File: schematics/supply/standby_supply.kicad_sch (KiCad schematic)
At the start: 38 parts, among them Q10 IRLML5203, U3 R7731, U4 EL817, U5 TL431DBV

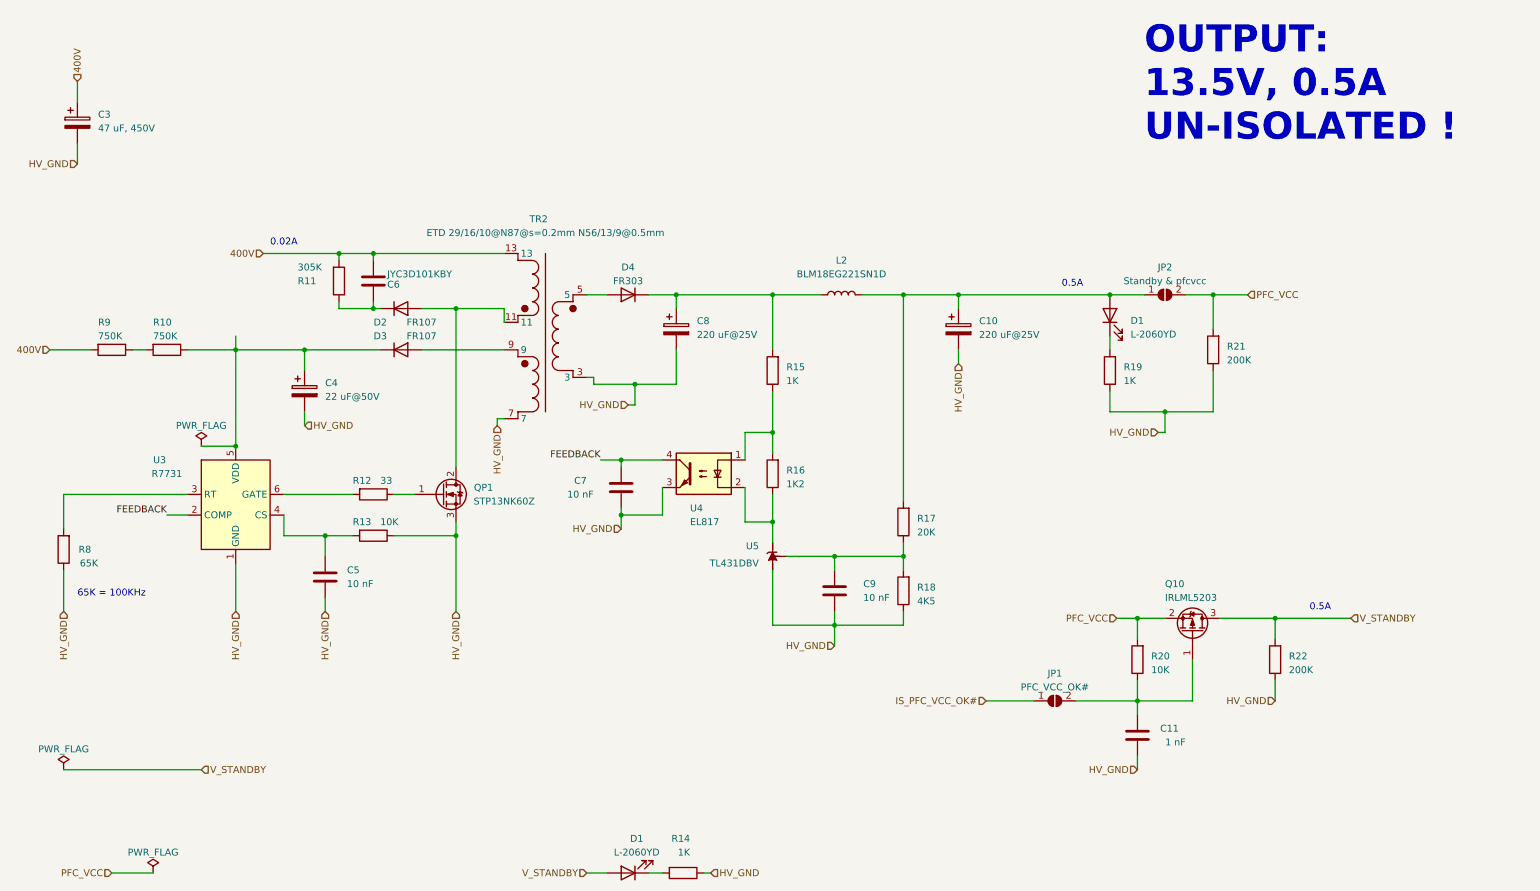
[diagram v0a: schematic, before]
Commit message: prepare to replace ina228 to attiny16+ina169(?). ina228 is an intresting chip, but its too expensive and Im not sure I can buy it on ali
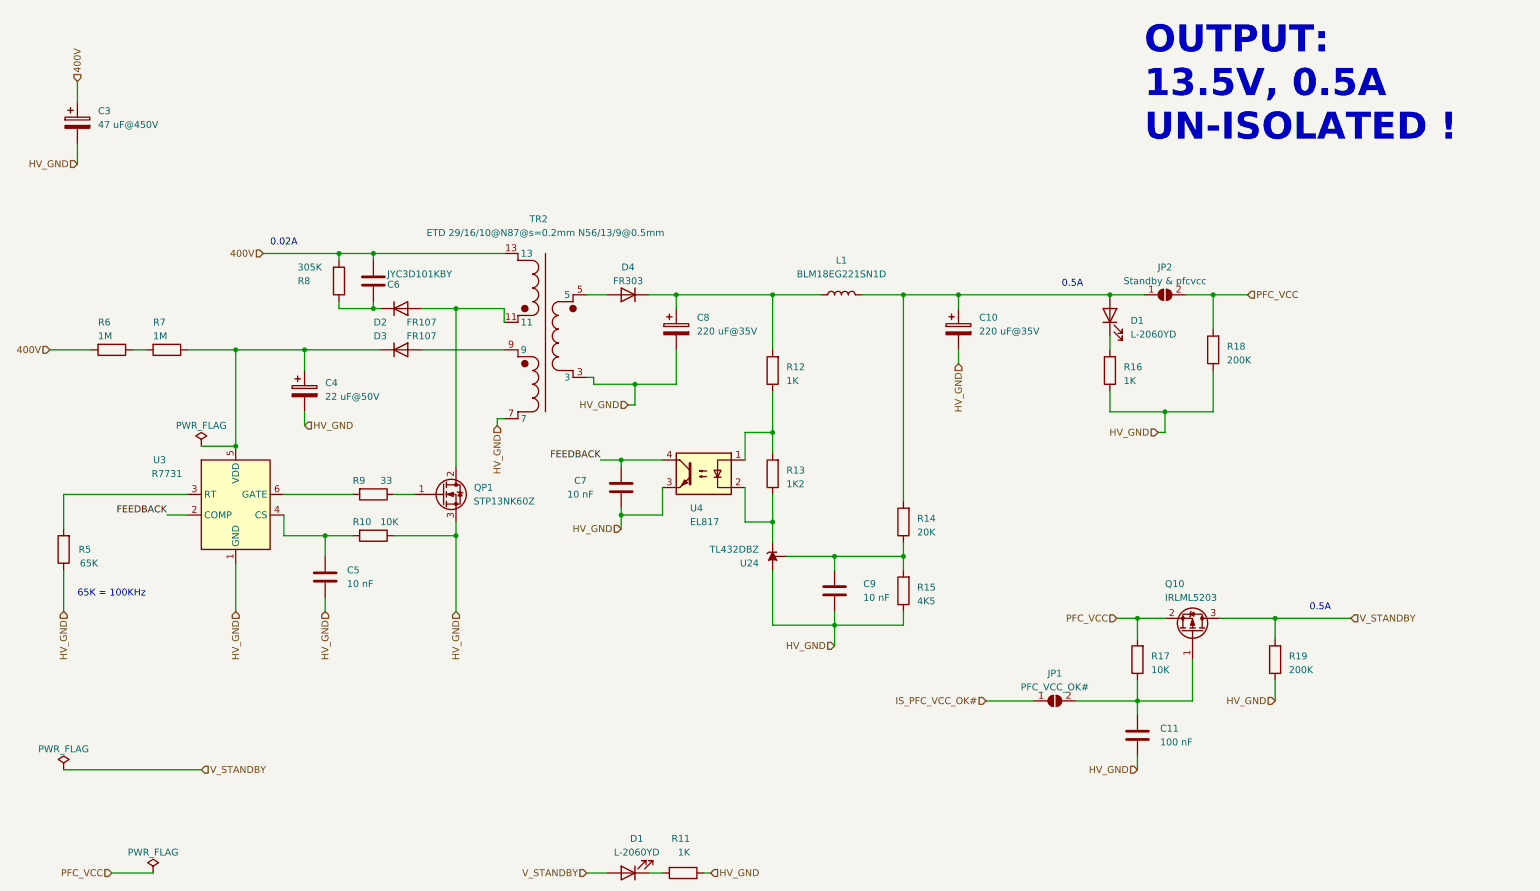
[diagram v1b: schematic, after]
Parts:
- removed U5: TL431DBV, Package_TO_SOT_SMD:SOT-23-5, symbol Reference_Voltage:TL431DBV
- added U24: TL432DBZ, Package_TO_SOT_SMD:SOT-23-3, symbol Reference_Voltage:TL432DBZ
- C10, C8: value 220 uF@25V -> 220 uF@35V
- C11: value 1 nF -> 100 nF
- C3: value 47 uF, 450V -> 47 uF@450V
- R6: renamed from R9; value 750K -> 1M
- R7: renamed from R10; value 750K -> 1M
- renumbered L2 to L1, R13 to R10, R14 to R11, R15 to R12, R16 to R13, R17 to R14, R18 to R15, R19 to R16, R20 to R17, R21 to R18, R22 to R19, R8 to R5, R11 to R8, R12 to R9
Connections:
- net HV_GND: now also U24.3 (A)
- net at C9.2, R14.1, R15.2: now also U24.1 (REF)
- net at R13.1, U4.2: now also U24.2 (K)

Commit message: Updated boards
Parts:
- D4: footprint Diode_THT:D_DO-201AD_P3.81mm_Vertical_KathodeUp -> Diode_THT:D_DO-201AD_P3.81mm_Vertical_AnodeUp
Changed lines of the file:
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@@
       (effects (font (size 1.27 1.27)))
     )
-    (property "Footprint" "Diode_THT:D_DO-201AD_P3.81mm_Vertical_KathodeUp" (at 127 67.31 0)
+    (property "Footprint" "Diode_THT:D_DO-201AD_P3.81mm_Vertical_AnodeUp" (at 127 67.31 0)
       (effects (font (size 1.27 1.27)) hide)
     )

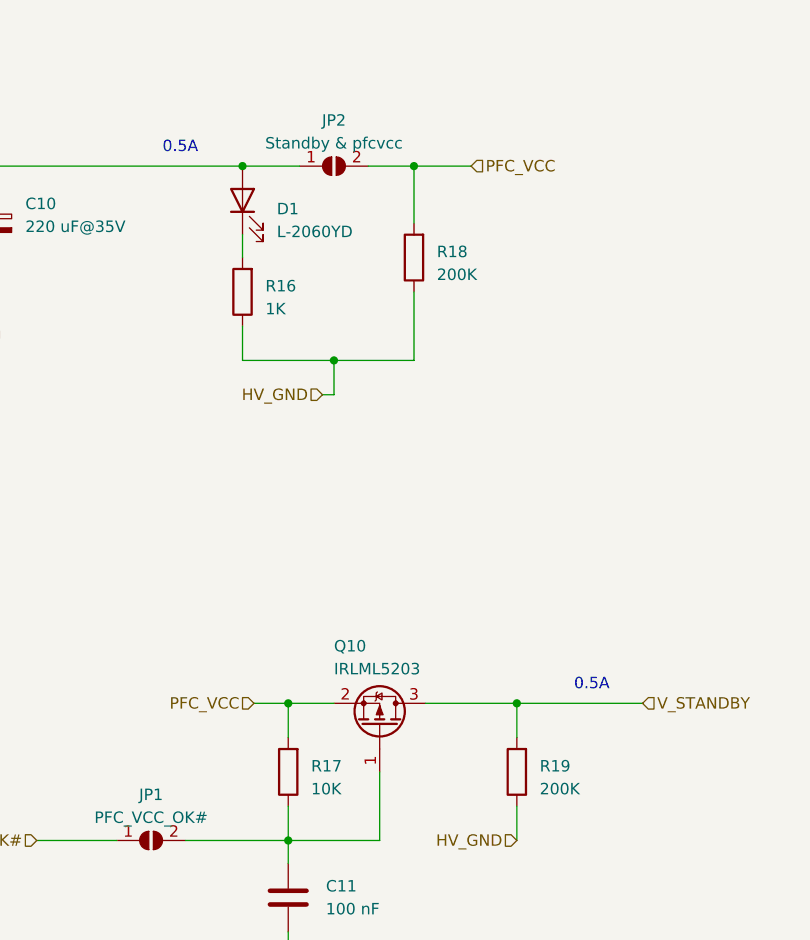
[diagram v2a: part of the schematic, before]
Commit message: little changes in schematics
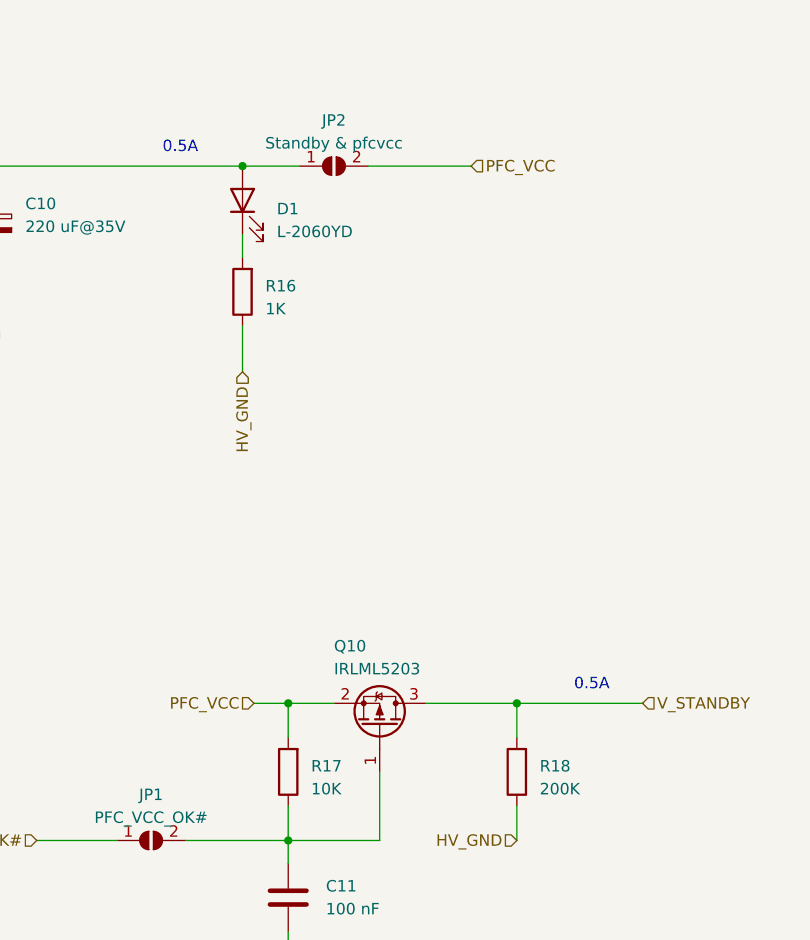
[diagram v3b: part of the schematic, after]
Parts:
- removed R18: 200K, Resistor_SMD:R_0805_2012Metric, symbol Device:R
- renumbered R19 to R18
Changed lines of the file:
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@@
   (junction (at 246.38 127) (diameter 0) (color 0 0 0 0)
   )
-  (junction (at 234.95 67.31) (diameter 0) (color 0 0 0 0)
-  )
   (junction (at 177.8 67.31) (diameter 0) (color 0 0 0 0)
   )
@@
   (junction (at 177.8 115.57) (diameter 0) (color 0 0 0 0)
   )
-  (junction (at 226.06 88.9) (diameter 0) (color 0 0 0 0)
-  )
   (junction (at 80.01 59.69) (diameter 0) (color 0 0 0 0)
   )
@@
     (stroke (width 0) (type default))
   )
-  (wire (pts (xy 226.06 92.71) (xy 226.06 88.9))
-    (stroke (width 0) (type default))
-  )
   (wire (pts (xy 119.38 82.55) (xy 120.65 82.55))
     (stroke (width 0) (type default))
   )
-  (wire (pts (xy 215.9 88.9) (xy 226.06 88.9))
-    (stroke (width 0) (type default))
-  )
   (wire (pts (xy 63.5 107.95) (xy 63.5 111.76))
     (stroke (width 0) (type default))
@@
     (stroke (width 0) (type default))
   )
-  (wire (pts (xy 224.79 92.71) (xy 226.06 92.71))
-    (stroke (width 0) (type default))
-  )
   (wire (pts (xy 25.4 39.37) (xy 25.4 43.18))
     (stroke (width 0) (type default))
@@
     (stroke (width 0) (type default))
   )
+  (wire (pts (xy 215.9 85.09) (xy 215.9 90.17))
+    (stroke (width 0) (type default))
+  )
   (wire (pts (xy 83.82 111.76) (xy 95.25 111.76))
     (stroke (width 0) (type default))
@@
     (stroke (width 0) (type default))
   )
-  (wire (pts (xy 234.95 67.31) (xy 241.3 67.31))
+  (wire (pts (xy 229.87 67.31) (xy 241.3 67.31))
     (stroke (width 0) (type default))
   )
@@
     (stroke (width 0) (type default))
   )
-  (wire (pts (xy 229.87 67.31) (xy 234.95 67.31))
-    (stroke (width 0) (type default))
-  )
   (wire (pts (xy 119.38 173.99) (xy 123.19 173.99))
     (stroke (width 0) (type default))
@@
     (stroke (width 0) (type default))
   )
-  (wire (pts (xy 226.06 88.9) (xy 234.95 88.9))
-    (stroke (width 0) (type default))
-  )
   (wire (pts (xy 25.4 27.94) (xy 25.4 31.75))
     (stroke (width 0) (type default))
@@
     (stroke (width 0) (type default))
   )
-  (wire (pts (xy 234.95 73.66) (xy 234.95 67.31))
-    (stroke (width 0) (type default))
-  )
   (wire (pts (xy 59.69 59.69) (xy 73.66 59.69))
     (stroke (width 0) (type default))
@@
     (stroke (width 0) (type default))
   )
-  (wire (pts (xy 215.9 85.09) (xy 215.9 88.9))
-    (stroke (width 0) (type default))
-  )
   (wire (pts (xy 88.9 69.85) (xy 95.25 69.85))
-    (stroke (width 0) (type default))
-  )
-  (wire (pts (xy 234.95 81.28) (xy 234.95 88.9))
     (stroke (width 0) (type default))
   )
@@
     (effects (font (size 1.27 1.27)) (justify right))
   )
-  (hierarchical_label "HV_GND" (shape input) (at 224.79 92.71 180) (fields_autoplaced)
+  (hierarchical_label "HV_GND" (shape input) (at 215.9 90.17 270) (fields_autoplaced)
     (effects (font (size 1.27 1.27)) (justify right))
   )
@@
   (symbol (lib_id "Device:R") (at 246.38 134.62 180) (unit 1)
     (in_bom yes) (on_board yes) (dnp no) (fields_autoplaced)
-    (property "Reference" "R19" (at 248.92 133.985 0)
+    (property "Reference" "R18" (at 248.92 133.985 0)
       (effects (font (size 1.27 1.27)) (justify right))
     )
@@
       (project "supply"
         (path "/1e139717-fcd1-4008-a6ea-4c993845e928/07fd8385-9dfd-4a86-92c6-a09da3061b53"
-          (reference "R19") (unit 1)
+          (reference "R18") (unit 1)
         )
       )
@@
         )
       )
-    )
-  )
-  (symbol (lib_id "Device:R") (at 234.95 77.47 180) (unit 1)
-    (in_bom yes) (on_board yes) (dnp no) (fields_autoplaced)
-    (property "Reference" "R18" (at 237.49 76.835 0)
-      (effects (font (size 1.27 1.27)) (justify right))
-    )
-    (property "Value" "200K" (at 237.49 79.375 0)
-      (effects (font (size 1.27 1.27)) (justify right))
-    )
-    (property "Footprint" "Resistor_SMD:R_0805_2012Metric" (at 236.728 77.47 90)
-      (effects (font (size 1.27 1.27)) hide)
-    )
-    (property "Datasheet" "~" (at 234.95 77.47 0)
-      (effects (font (size 1.27 1.27)) hide)
-    )
-    (pin "1")
-    (pin "2")
-    (instances
-      (project "supply"
-        (path "/1e139717-fcd1-4008-a6ea-4c993845e928/07fd8385-9dfd-4a86-92c6-a09da3061b53"
-          (reference "R18") (unit 1)
-        )
-      )

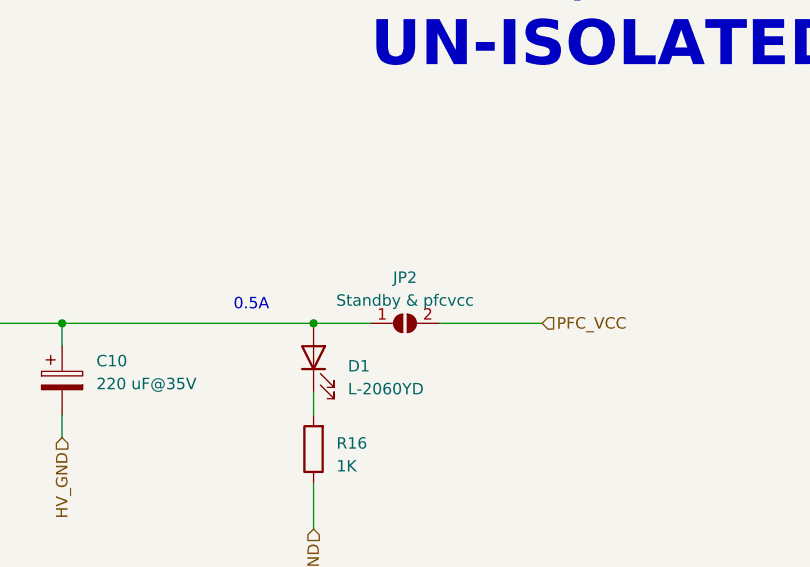
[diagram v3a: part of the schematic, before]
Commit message: prepare to add current measurement for a middle-current 5V and 3.3V lines
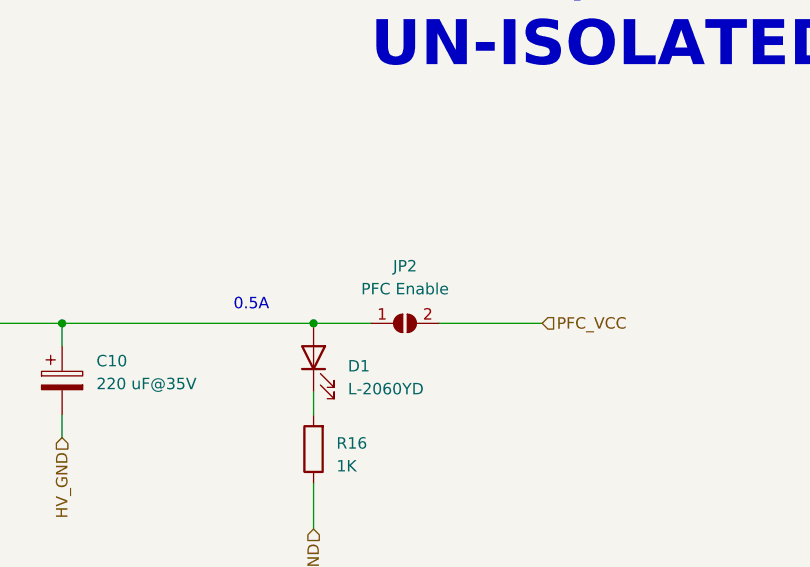
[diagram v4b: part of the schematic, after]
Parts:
- JP2: value Standby & pfcvcc -> PFC Enable
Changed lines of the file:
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@@
   (symbol (lib_id "Jumper:SolderJumper_2_Open") (at 226.06 67.31 0) (unit 1)
     (in_bom yes) (on_board yes) (dnp no) (fields_autoplaced)
-    (property "Reference" "JP2" (at 226.06 62.23 0)
+    (property "Reference" "JP2" (at 226.06 60.96 0)
       (effects (font (size 1.27 1.27)))
     )
-    (property "Value" "Standby & pfcvcc" (at 226.06 64.77 0)
+    (property "Value" "PFC Enable" (at 226.06 63.5 0)
       (effects (font (size 1.27 1.27)))
     )

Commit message: Board prepared to order
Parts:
- R15: value 4K5 -> 4K7
- R5: value 65K -> 62K
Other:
- note added: "62K ~ 104...105KHz"
- note removed: "65K = 100KHz"
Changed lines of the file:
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@@
     (effects (font (size 1.27 1.27)) (justify left bottom))
   )
-  (text "65K = 100KHz" (at 25.4 123.19 0)
+  (text "62K ~ 104...105KHz" (at 25.4 123.19 0)
     (effects (font (size 1.27 1.27)) (justify left bottom))
   )
@@
       (effects (font (size 1.27 1.27)) (justify left))
     )
-    (property "Value" "65K" (at 29.21 116.84 0)
+    (property "Value" "62K" (at 29.21 116.84 0)
       (effects (font (size 1.27 1.27)) (justify left))
     )
@@
   (symbol (lib_id "Device:R") (at 177.8 121.92 180) (unit 1)
     (in_bom yes) (on_board yes) (dnp no) (fields_autoplaced)
-    (property "Reference" "R15" (at 180.34 121.285 0)
-      (effects (font (size 1.27 1.27)) (justify right))
-    )
-    (property "Value" "4K5" (at 180.34 123.825 0)
-      (effects (font (size 1.27 1.27)) (justify right))
-    )
+    (property "Reference" "R15" (at 180.34 120.65 0)
+      (effects (font (size 1.27 1.27)) (justify right))
+    )
+    (property "Value" "4K7" (at 180.34 123.19 0)
+      (effects (font (size 1.27 1.27)) (justify right))
+    )

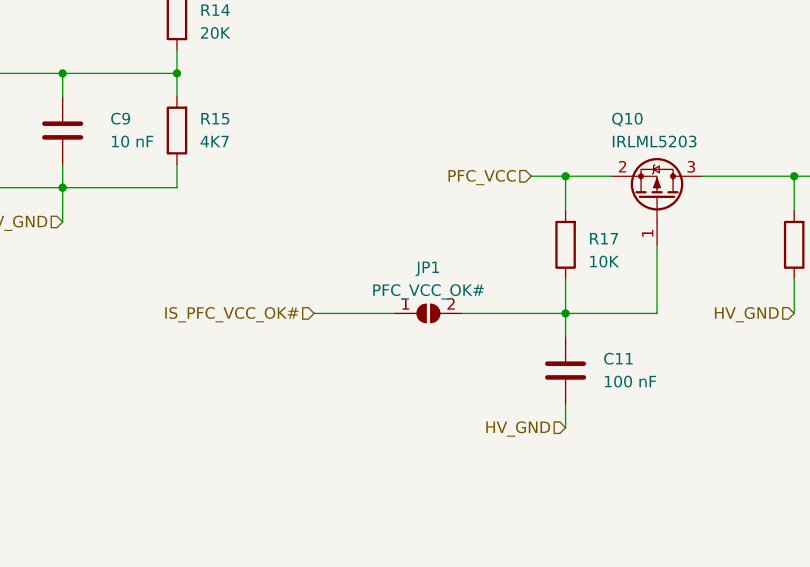
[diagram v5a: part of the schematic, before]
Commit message: One board settings changed from 4-layers to 2-layers to reduce it's price
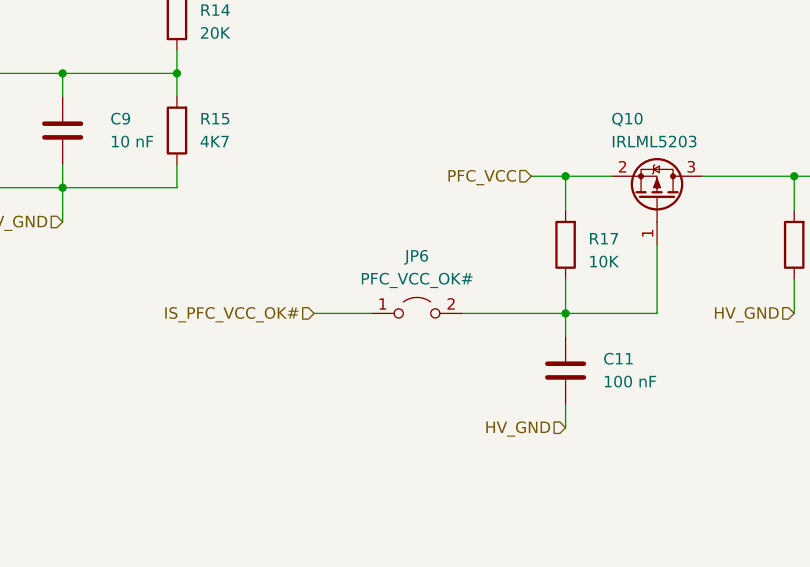
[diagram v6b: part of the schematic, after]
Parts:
- removed JP1: PFC_VCC_OK#, Jumper:SolderJumper-2_P1.3mm_Open_TrianglePad1.0x1.5mm, symbol Jumper:SolderJumper_2_Open
- added JP6: PFC_VCC_OK#, TestPoint:TestPoint_2Pads_Pitch2.54mm_Drill0.8mm, symbol Jumper:Jumper_2_Open
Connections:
- net IS_PFC_VCC_OK#: now also JP6.1 (A)
- net at C11.2, Q10.1 (G), R17.1: now also JP6.2 (B)
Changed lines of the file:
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@@
+    (stroke (width 0) (type default))
+  )
+  (wire (pts (xy 193.04 142.24) (xy 199.39 142.24))
     (stroke (width 0) (type default))
   )
@@
   )
   (wire (pts (xy 153.67 128.27) (xy 153.67 118.11))
-    (stroke (width 0) (type default))
-  )
-  (wire (pts (xy 193.04 142.24) (xy 201.93 142.24))
     (stroke (width 0) (type default))
   )
@@
   (hierarchical_label "PFC_VCC" (shape input) (at 241.3 67.31 0) (fields_autoplaced)
     (effects (font (size 1.27 1.27)) (justify left))
-  )
-  (symbol (lib_id "Jumper:SolderJumper_2_Open") (at 205.74 142.24 0) (unit 1)
-    (in_bom yes) (on_board yes) (dnp no) (fields_autoplaced)
-    (property "Reference" "JP1" (at 205.74 137.16 0)
-      (effects (font (size 1.27 1.27)))
-    )
-    (property "Value" "PFC_VCC_OK#" (at 205.74 139.7 0)
-      (effects (font (size 1.27 1.27)))
-    )
-    (property "Footprint" "Jumper:SolderJumper-2_P1.3mm_Open_TrianglePad1.0x1.5mm" (at 205.74 142.24 0)
-      (effects (font (size 1.27 1.27)) hide)
-    )
-    (property "Datasheet" "~" (at 205.74 142.24 0)
-      (effects (font (size 1.27 1.27)) hide)
-    )
-    (pin "1")
-    (pin "2")
-    (instances
-      (project "supply"
-        (path "/1e139717-fcd1-4008-a6ea-4c993845e928/07fd8385-9dfd-4a86-92c6-a09da3061b53"
-          (reference "JP1") (unit 1)
-        )
-      )
-    )
   )
   (symbol (lib_id "Device:D") (at 85.09 77.47 0) (unit 1)
@@
         )
       )
+    )
+  )
+  (symbol (lib_id "Jumper:Jumper_2_Open") (at 204.47 142.24 0) (unit 1)
+    (in_bom yes) (on_board yes) (dnp no) (fields_autoplaced)
+    (property "Reference" "JP6" (at 204.47 135.89 0)
+      (effects (font (size 1.27 1.27)))
+    )
+    (property "Value" "PFC_VCC_OK#" (at 204.47 138.43 0)
+      (effects (font (size 1.27 1.27)))
+    )
+    (property "Footprint" "TestPoint:TestPoint_2Pads_Pitch2.54mm_Drill0.8mm" (at 204.47 142.24 0)
+      (effects (font (size 1.27 1.27)) hide)
+    )
+    (property "Datasheet" "~" (at 204.47 142.24 0)
+      (effects (font (size 1.27 1.27)) hide)
+    )
+    (pin "1")
+    (pin "2")
+    (instances
+      (project "supply"
+        (path "/1e139717-fcd1-4008-a6ea-4c993845e928/ce2ff71a-422a-4b17-921a-2433d38ec044"
+          (reference "JP6") (unit 1)
+        )
+        (path "/1e139717-fcd1-4008-a6ea-4c993845e928/07fd8385-9dfd-4a86-92c6-a09da3061b53"
+          (reference "JP7") (unit 1)
+        )
+      )
